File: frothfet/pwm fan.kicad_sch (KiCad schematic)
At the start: 3 parts, among them J14 FAN, Q10 AO3400A

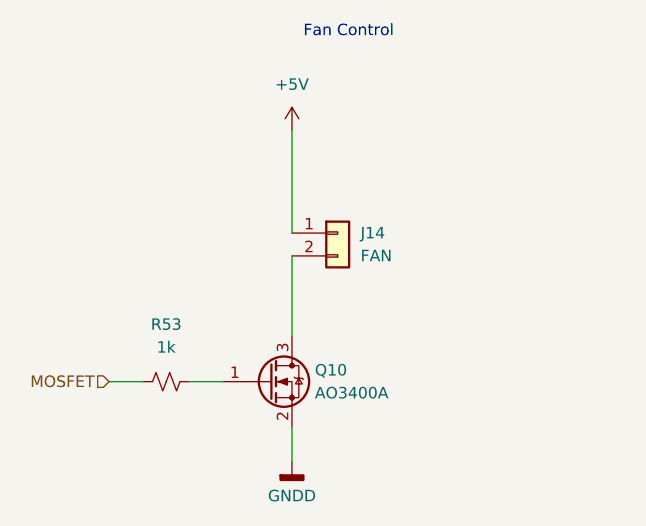
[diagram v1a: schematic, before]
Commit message: updated the dummy load schematic.
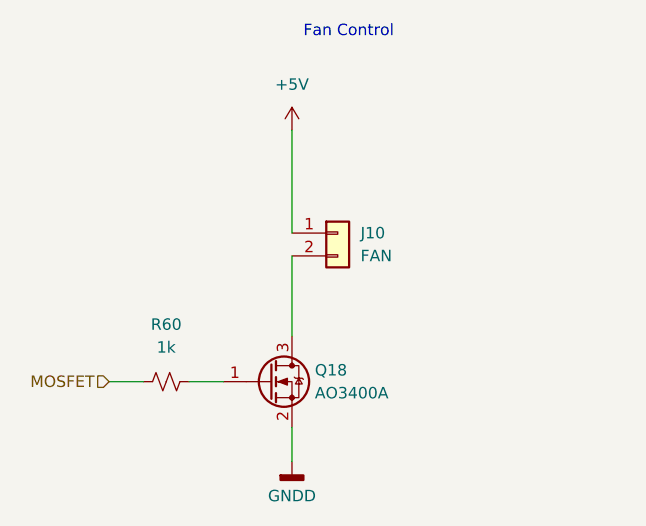
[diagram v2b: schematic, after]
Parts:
- renumbered J14 to J10, Q10 to Q18, R53 to R60
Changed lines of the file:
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@@
 		(dnp no)
 		(fields_autoplaced yes)
-		(property "Reference" "#PWR060"
+		(property "Reference" "#PWR089"
 			(at 133.35 111.76 0)
 			(effects
@@
 			(project "8ch-mosfet"
 				(path "/c83c6236-96e9-46ad-9d7a-9e2efa4a7966/02f6e629-b0e2-41e8-b2e4-f0e125a92a71"
-					(reference "#PWR060")
-					(unit 1)
-				)
-				(path "/c83c6236-96e9-46ad-9d7a-9e2efa4a7966/ad82ad0c-2ba8-4934-bb2a-ed6e11658eb2"
-					(reference "#PWR057")
+					(reference "#PWR089")
+					(unit 1)
+				)
+				(path "/c83c6236-96e9-46ad-9d7a-9e2efa4a7966/ad82ad0c-2ba8-4934-bb2a-ed6e11658eb2"
+					(reference "#PWR087")
 					(unit 1)
 				)
@@
 		(dnp no)
 		(fields_autoplaced yes)
-		(property "Reference" "J14"
+		(property "Reference" "J10"
 			(at 140.97 80.0099 0)
 			(effects
@@
 			(project ""
 				(path "/c83c6236-96e9-46ad-9d7a-9e2efa4a7966/02f6e629-b0e2-41e8-b2e4-f0e125a92a71"
-					(reference "J14")
-					(unit 1)
-				)
-				(path "/c83c6236-96e9-46ad-9d7a-9e2efa4a7966/ad82ad0c-2ba8-4934-bb2a-ed6e11658eb2"
-					(reference "J13")
+					(reference "J10")
+					(unit 1)
+				)
+				(path "/c83c6236-96e9-46ad-9d7a-9e2efa4a7966/ad82ad0c-2ba8-4934-bb2a-ed6e11658eb2"
+					(reference "J9")
 					(unit 1)
 				)
@@
 		(on_board yes)
 		(dnp no)
-		(property "Reference" "Q10"
+		(property "Reference" "Q18"
 			(at 135.89 95.25 0)
 			(effects
@@
 			(project "8ch-mosfet"
 				(path "/c83c6236-96e9-46ad-9d7a-9e2efa4a7966/02f6e629-b0e2-41e8-b2e4-f0e125a92a71"
-					(reference "Q10")
-					(unit 1)
-				)
-				(path "/c83c6236-96e9-46ad-9d7a-9e2efa4a7966/ad82ad0c-2ba8-4934-bb2a-ed6e11658eb2"
-					(reference "Q9")
+					(reference "Q18")
+					(unit 1)
+				)
+				(path "/c83c6236-96e9-46ad-9d7a-9e2efa4a7966/ad82ad0c-2ba8-4934-bb2a-ed6e11658eb2"
+					(reference "Q17")
 					(unit 1)
 				)
@@
 		(dnp no)
 		(fields_autoplaced yes)
-		(property "Reference" "#PWR059"
+		(property "Reference" "#PWR088"
 			(at 133.35 72.39 0)
 			(effects
@@
 			(project "8ch-mosfet"
 				(path "/c83c6236-96e9-46ad-9d7a-9e2efa4a7966/02f6e629-b0e2-41e8-b2e4-f0e125a92a71"
-					(reference "#PWR059")
-					(unit 1)
-				)
-				(path "/c83c6236-96e9-46ad-9d7a-9e2efa4a7966/ad82ad0c-2ba8-4934-bb2a-ed6e11658eb2"
-					(reference "#PWR056")
+					(reference "#PWR088")
+					(unit 1)
+				)
+				(path "/c83c6236-96e9-46ad-9d7a-9e2efa4a7966/ad82ad0c-2ba8-4934-bb2a-ed6e11658eb2"
+					(reference "#PWR086")
 					(unit 1)
 				)
@@
 		(dnp no)
 		(fields_autoplaced yes)
-		(property "Reference" "R53"
+		(property "Reference" "R60"
 			(at 119.38 90.17 90)
 			(effects
@@
 			(project "8ch-mosfet"
 				(path "/c83c6236-96e9-46ad-9d7a-9e2efa4a7966/02f6e629-b0e2-41e8-b2e4-f0e125a92a71"
-					(reference "R53")
-					(unit 1)
-				)
-				(path "/c83c6236-96e9-46ad-9d7a-9e2efa4a7966/ad82ad0c-2ba8-4934-bb2a-ed6e11658eb2"
-					(reference "R51")
-					(unit 1)
-				)
+					(reference "R60")
+					(unit 1)
+				)
+				(path "/c83c6236-96e9-46ad-9d7a-9e2efa4a7966/ad82ad0c-2ba8-4934-bb2a-ed6e11658eb2"
+					(reference "R59")
+					(unit 1)
+				)

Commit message: started work on rev e, looking clean at 13mm
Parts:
- renumbered J10 to J2, R60 to R68
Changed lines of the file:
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@@
 		(dnp no)
 		(fields_autoplaced yes)
-		(property "Reference" "J10"
+		(property "Reference" "J2"
 			(at 140.97 80.0099 0)
 			(effects
@@
 			(project ""
 				(path "/c83c6236-96e9-46ad-9d7a-9e2efa4a7966/02f6e629-b0e2-41e8-b2e4-f0e125a92a71"
-					(reference "J10")
+					(reference "J2")
 					(unit 1)
 				)
 				(path "/c83c6236-96e9-46ad-9d7a-9e2efa4a7966/ad82ad0c-2ba8-4934-bb2a-ed6e11658eb2"
-					(reference "J9")
+					(reference "J1")
 					(unit 1)
 				)
@@
 		(dnp no)
 		(fields_autoplaced yes)
-		(property "Reference" "R60"
+		(property "Reference" "R68"
 			(at 119.38 90.17 90)
 			(effects
@@
 			(project "8ch-mosfet"
 				(path "/c83c6236-96e9-46ad-9d7a-9e2efa4a7966/02f6e629-b0e2-41e8-b2e4-f0e125a92a71"
-					(reference "R60")
+					(reference "R68")
 					(unit 1)
 				)
 				(path "/c83c6236-96e9-46ad-9d7a-9e2efa4a7966/ad82ad0c-2ba8-4934-bb2a-ed6e11658eb2"
-					(reference "R59")
-					(unit 1)
-				)
+					(reference "R67")
+					(unit 1)
+				)

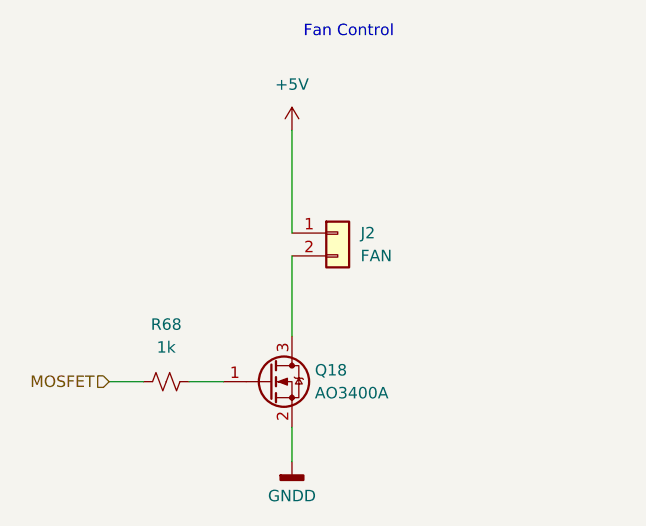
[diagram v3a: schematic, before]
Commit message: changed to 0603 and various tweaks
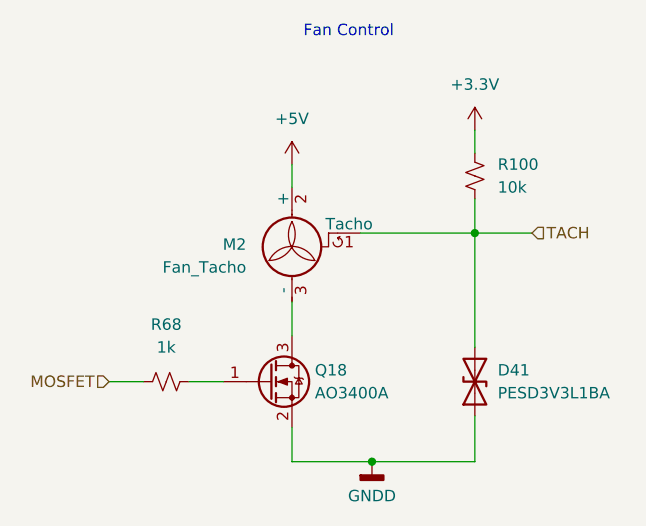
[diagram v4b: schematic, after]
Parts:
- removed J2: FAN, Connector_JST:JST_PH_B2B-PH-SM4-TB_1x02-1MP_P2.00mm_Vertical, symbol Connector_Generic:Conn_01x02
- added D41: PESD3V3L1BA, Diode_SMD:D_SOD-323, symbol Device:D_TVS
- added M2: Fan_Tacho, Connector:FanPinHeader_1x03_P2.54mm_Vertical, symbol Motor:Fan_Tacho
- added R100: 10k, Resistor_SMD:R_0603_1608Metric, symbol Device:R_Small_US
- R68: footprint Resistor_SMD:R_0805_2012Metric_Pad1.20x1.40mm_HandSolder -> Resistor_SMD:R_0603_1608Metric
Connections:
- net +5V: now also M2.2 (+)
- net GNDD: now also D41.1 (A1)
- net at Q18.3 (D): now also M2.3 (-)
- new net +3.3V: R100.2
- new net TACH: D41.2 (A2), M2.1 (Tacho), R100.1

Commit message: updated to kicad v9
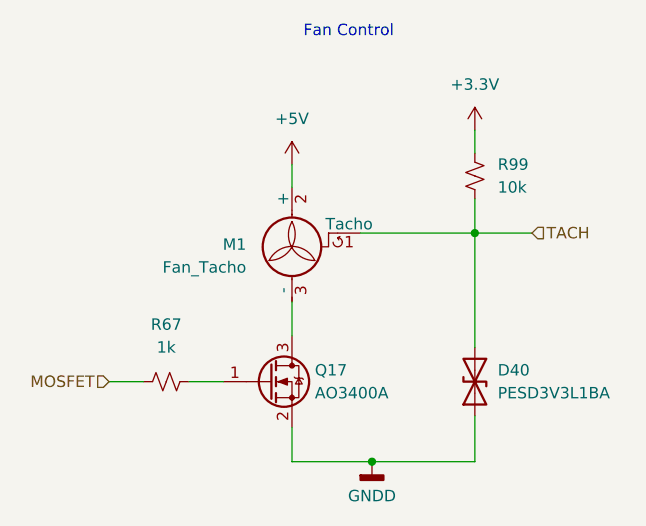
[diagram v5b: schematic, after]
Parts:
- renumbered D41 to D40, M2 to M1, Q18 to Q17, R68 to R67, R100 to R99
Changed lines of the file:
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@@
 (kicad_sch
-	(version 20231120)
+	(version 20250114)
 	(generator "eeschema")
-	(generator_version "8.0")
+	(generator_version "9.0")
 	(paper "A4")
 	(title_block
@@
 		(company "https://github.com/hoeken/frothfet")
 	)
+	(text "Fan Control"
+		(exclude_from_sim no)
+		(at 134.62 58.42 0)
+		(effects
+			(font
+				(size 1.27 1.27)
+			)
+			(justify left bottom)
+		)
+	)
 	(junction
 		(at 142.24 105.41)
@@
 		)
 	)
-	(text "Fan Control"
-		(exclude_from_sim no)
-		(at 134.62 58.42 0)
+	(hierarchical_label "TACH"
+		(shape input)
+		(at 160.02 80.01 0)
 		(effects
 			(font
 				(size 1.27 1.27)
 			)
-			(justify left bottom)
-		)
-	)
-	(hierarchical_label "TACH"
-		(shape input)
-		(at 160.02 80.01 0)
-		(fields_autoplaced yes)
-		(effects
-			(font
-				(size 1.27 1.27)
-			)
 			(justify left)
 		)
@@
 		(shape input)
 		(at 113.03 96.52 180)
-		(fields_autoplaced yes)
 		(effects
 			(font
@@
 		(on_board yes)
 		(dnp no)
-		(property "Reference" "D41"
+		(property "Reference" "D40"
 			(at 156.21 95.25 90)
 			(effects
@@
 		(dnp no)
 		(fields_autoplaced yes)
-		(property "Reference" "R100"
+		(property "Reference" "R99"
 			(at 156.21 72.39 0)
 			(effects
@@
 		(dnp no)
 		(fields_autoplaced yes)
-		(property "Reference" "#PWR089"
+		(property "Reference" "#PWR087"
 			(at 142.24 111.76 0)
 			(effects
@@
 		(on_board yes)
 		(dnp no)
-		(property "Reference" "Q18"
+		(property "Reference" "Q17"
 			(at 135.89 95.25 0)
 			(effects
@@
 		(dnp no)
 		(fields_autoplaced yes)
-		(property "Reference" "#PWR0118"
+		(property "Reference" "#PWR0117"
 			(at 153.67 72.39 0)
 			(effects
@@
 		(dnp no)
 		(fields_autoplaced yes)
-		(property "Reference" "M2"
+		(property "Reference" "M1"
 			(at 128.27 81.2799 0)
 			(effects
@@
 		(dnp no)
 		(fields_autoplaced yes)
-		(property "Reference" "#PWR088"
+		(property "Reference" "#PWR086"
 			(at 133.35 76.2 0)
 			(effects
@@
 		(dnp no)
 		(fields_autoplaced yes)
-		(property "Reference" "R68"
+		(property "Reference" "R67"
 			(at 119.38 90.17 90)
 			(effects

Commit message: worked on the bom and footprint placement
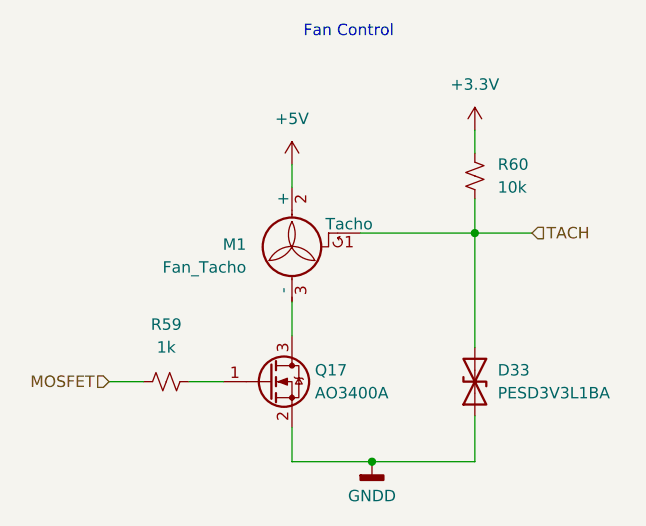
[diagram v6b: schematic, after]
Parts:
- M1: LCSC (none) -> C86503
- R59: renamed from R67; LCSC C95781 -> (none)
- renumbered D40 to D33, R99 to R60
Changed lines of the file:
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@@
 		(on_board yes)
 		(dnp no)
-		(property "Reference" "D40"
+		(property "Reference" "D33"
 			(at 156.21 95.25 90)
 			(effects
@@
 			(project "frothfet"
 				(path "/c83c6236-96e9-46ad-9d7a-9e2efa4a7966/02f6e629-b0e2-41e8-b2e4-f0e125a92a71"
-					(reference "D41")
-					(unit 1)
-				)
-				(path "/c83c6236-96e9-46ad-9d7a-9e2efa4a7966/ad82ad0c-2ba8-4934-bb2a-ed6e11658eb2"
-					(reference "D40")
+					(reference "D34")
+					(unit 1)
+				)
+				(path "/c83c6236-96e9-46ad-9d7a-9e2efa4a7966/ad82ad0c-2ba8-4934-bb2a-ed6e11658eb2"
+					(reference "D33")
 					(unit 1)
 				)
@@
 		(dnp no)
 		(fields_autoplaced yes)
-		(property "Reference" "R99"
+		(property "Reference" "R60"
 			(at 156.21 72.39 0)
 			(effects
@@
 			(project "frothfet"
 				(path "/c83c6236-96e9-46ad-9d7a-9e2efa4a7966/02f6e629-b0e2-41e8-b2e4-f0e125a92a71"
-					(reference "R100")
-					(unit 1)
-				)
-				(path "/c83c6236-96e9-46ad-9d7a-9e2efa4a7966/ad82ad0c-2ba8-4934-bb2a-ed6e11658eb2"
-					(reference "R99")
+					(reference "R62")
+					(unit 1)
+				)
+				(path "/c83c6236-96e9-46ad-9d7a-9e2efa4a7966/ad82ad0c-2ba8-4934-bb2a-ed6e11658eb2"
+					(reference "R60")
 					(unit 1)
 				)
@@
 		(dnp no)
 		(fields_autoplaced yes)
-		(property "Reference" "#PWR087"
+		(property "Reference" "#PWR078"
 			(at 142.24 111.76 0)
 			(effects
@@
 			(project "8ch-mosfet"
 				(path "/c83c6236-96e9-46ad-9d7a-9e2efa4a7966/02f6e629-b0e2-41e8-b2e4-f0e125a92a71"
-					(reference "#PWR089")
-					(unit 1)
-				)
-				(path "/c83c6236-96e9-46ad-9d7a-9e2efa4a7966/ad82ad0c-2ba8-4934-bb2a-ed6e11658eb2"
-					(reference "#PWR087")
+					(reference "#PWR081")
+					(unit 1)
+				)
+				(path "/c83c6236-96e9-46ad-9d7a-9e2efa4a7966/ad82ad0c-2ba8-4934-bb2a-ed6e11658eb2"
+					(reference "#PWR078")
 					(unit 1)
 				)
@@
 		(dnp no)
 		(fields_autoplaced yes)
-		(property "Reference" "#PWR0117"
+		(property "Reference" "#PWR079"
 			(at 153.67 72.39 0)
 			(effects
@@
 			(project "frothfet"
 				(path "/c83c6236-96e9-46ad-9d7a-9e2efa4a7966/02f6e629-b0e2-41e8-b2e4-f0e125a92a71"
-					(reference "#PWR0118")
-					(unit 1)
-				)
-				(path "/c83c6236-96e9-46ad-9d7a-9e2efa4a7966/ad82ad0c-2ba8-4934-bb2a-ed6e11658eb2"
-					(reference "#PWR0117")
+					(reference "#PWR082")
+					(unit 1)
+				)
+				(path "/c83c6236-96e9-46ad-9d7a-9e2efa4a7966/ad82ad0c-2ba8-4934-bb2a-ed6e11658eb2"
+					(reference "#PWR079")
 					(unit 1)
 				)
@@
 			)
 		)
+		(property "LCSC" "C86503"
+			(at 133.35 80.01 0)
+			(effects
+				(font
+					(size 1.27 1.27)
+				)
+				(hide yes)
+			)
+		)
 		(pin "3"
 		)
@@
 		(dnp no)
 		(fields_autoplaced yes)
-		(property "Reference" "#PWR086"
+		(property "Reference" "#PWR077"
 			(at 133.35 76.2 0)
 			(effects
@@
 			(project "8ch-mosfet"
 				(path "/c83c6236-96e9-46ad-9d7a-9e2efa4a7966/02f6e629-b0e2-41e8-b2e4-f0e125a92a71"
-					(reference "#PWR088")
-					(unit 1)
-				)
-				(path "/c83c6236-96e9-46ad-9d7a-9e2efa4a7966/ad82ad0c-2ba8-4934-bb2a-ed6e11658eb2"
-					(reference "#PWR086")
+					(reference "#PWR080")
+					(unit 1)
+				)
+				(path "/c83c6236-96e9-46ad-9d7a-9e2efa4a7966/ad82ad0c-2ba8-4934-bb2a-ed6e11658eb2"
+					(reference "#PWR077")
 					(unit 1)
 				)
@@
 		(dnp no)
 		(fields_autoplaced yes)
-		(property "Reference" "R67"
+		(property "Reference" "R59"
 			(at 119.38 90.17 90)
 			(effects
@@
 			)
 		)
-		(property "LCSC" "C95781"
+		(property "LCSC" ""
 			(at 119.38 96.52 0)
 			(effects
@@
 			(project "8ch-mosfet"
 				(path "/c83c6236-96e9-46ad-9d7a-9e2efa4a7966/02f6e629-b0e2-41e8-b2e4-f0e125a92a71"
-					(reference "R68")
-					(unit 1)
-				)
-				(path "/c83c6236-96e9-46ad-9d7a-9e2efa4a7966/ad82ad0c-2ba8-4934-bb2a-ed6e11658eb2"
-					(reference "R67")
-					(unit 1)
-				)
+					(reference "R61")
+					(unit 1)
+				)
+				(path "/c83c6236-96e9-46ad-9d7a-9e2efa4a7966/ad82ad0c-2ba8-4934-bb2a-ed6e11658eb2"
+					(reference "R59")
+					(unit 1)
+				)
